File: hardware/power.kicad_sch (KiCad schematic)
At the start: 19 parts, among them U1 ECP5U_12_CABGA256, U2 TLV62569DBV, U3 TLV62569DBV, U4 TLV62569DBV

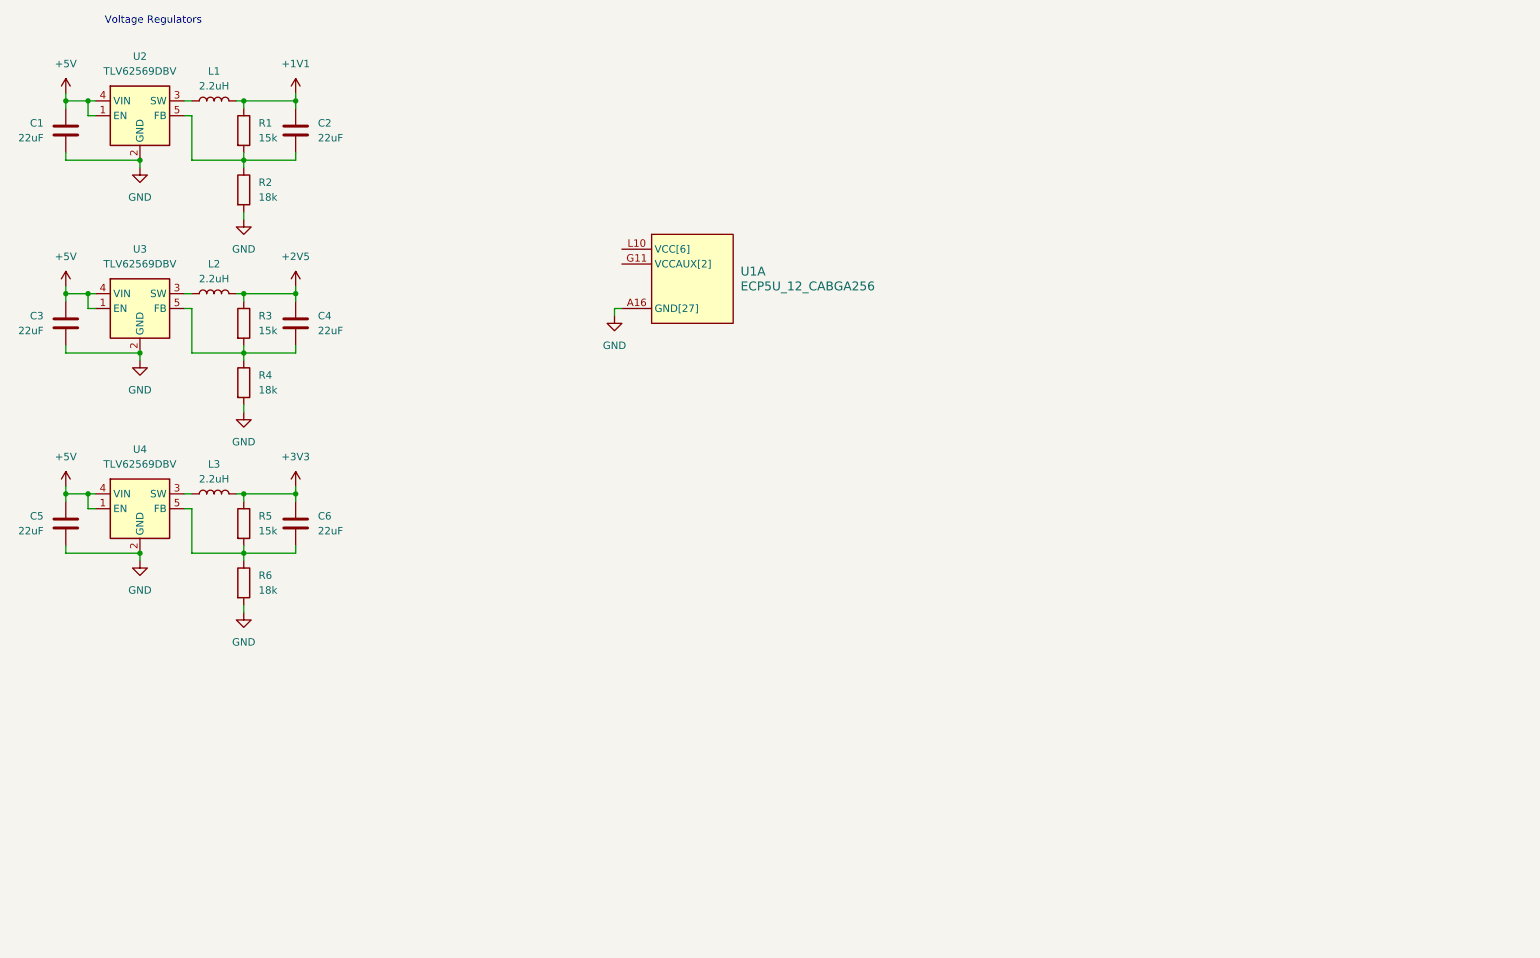
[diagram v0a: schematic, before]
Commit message: Routed most of sdram
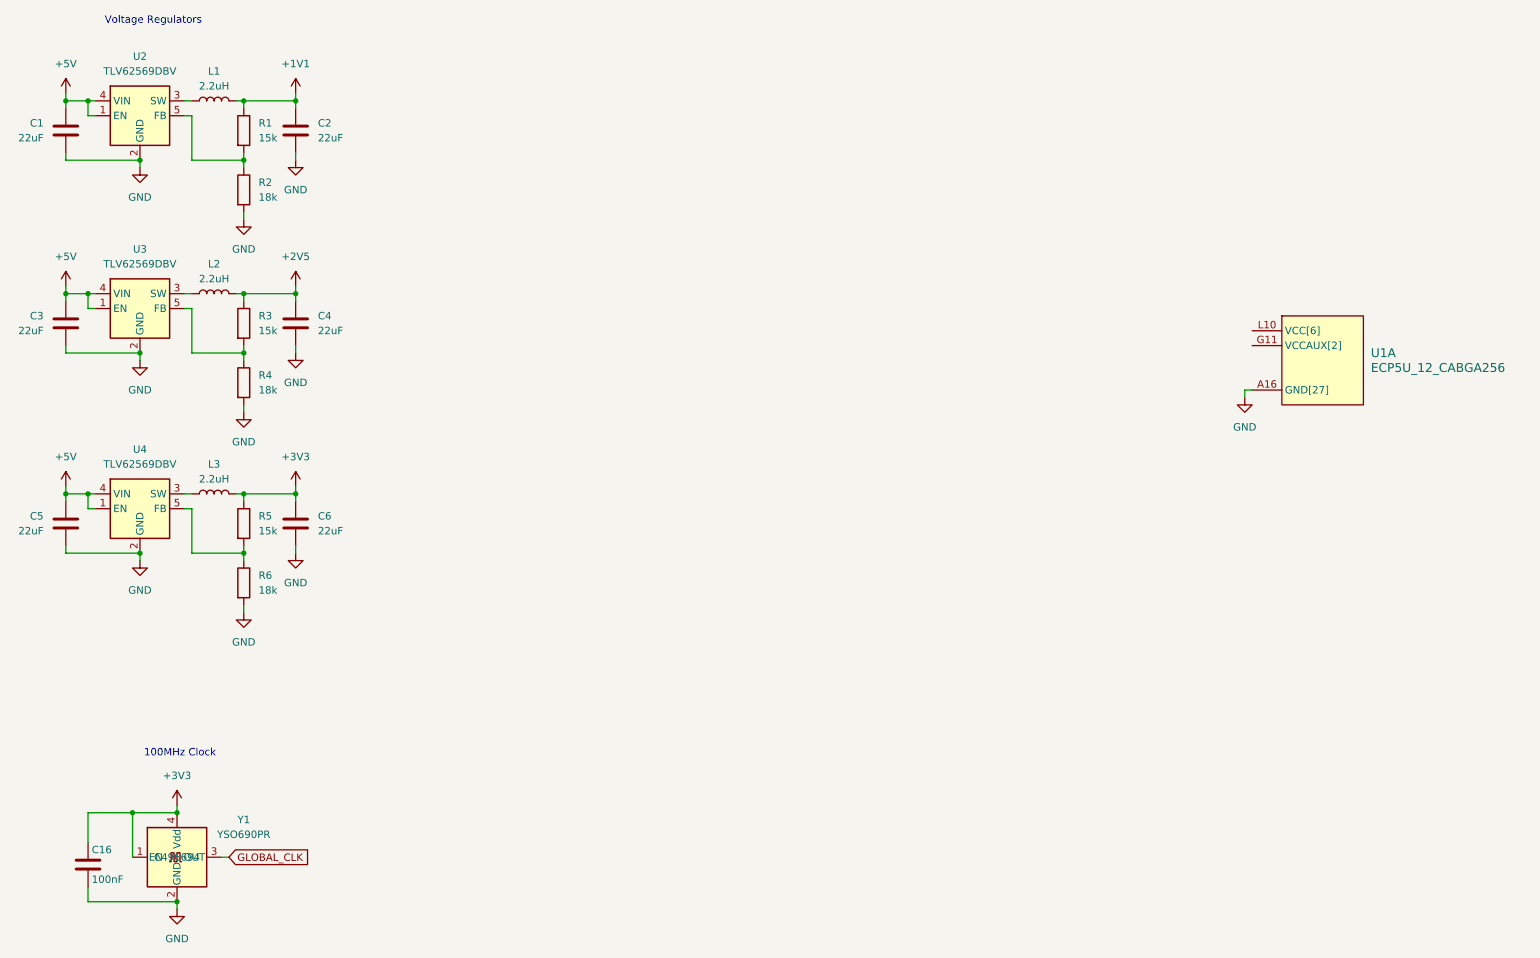
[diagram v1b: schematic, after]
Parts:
- added C16: 100nF, Capacitor_SMD:C_0402_1005Metric, symbol Device:C
- added Y1: YSO690PR, Oscillator:Oscillator_SMD_SiT_PQFN-4Pin_3.2x2.5mm, symbol Oscillator:ASE-xxxMHz
- R1, R2, R3, R4, R5, R6: footprint Resistor_SMD:R_0603_1608Metric -> Resistor_SMD:R_0402_1005Metric
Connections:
- net +3V3: now also C16.1, Y1.1 (EN), Y1.4 (Vdd)
- net GND: now also C2.2, C4.2, C6.2, C16.2, Y1.2 (GND)
- net at R1.2, R2.1, U2.5 (FB): no longer C2.2
- net at R5.2, R6.1, U4.5 (FB): no longer C6.2
- net at R3.2, R4.1, U3.5 (FB): no longer C4.2
- new net GLOBAL_CLK: Y1.3 (OUT)
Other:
- note added: "100MHz Clock"
- moved on the sheet: U1A

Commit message: Added the decoupling capacitors
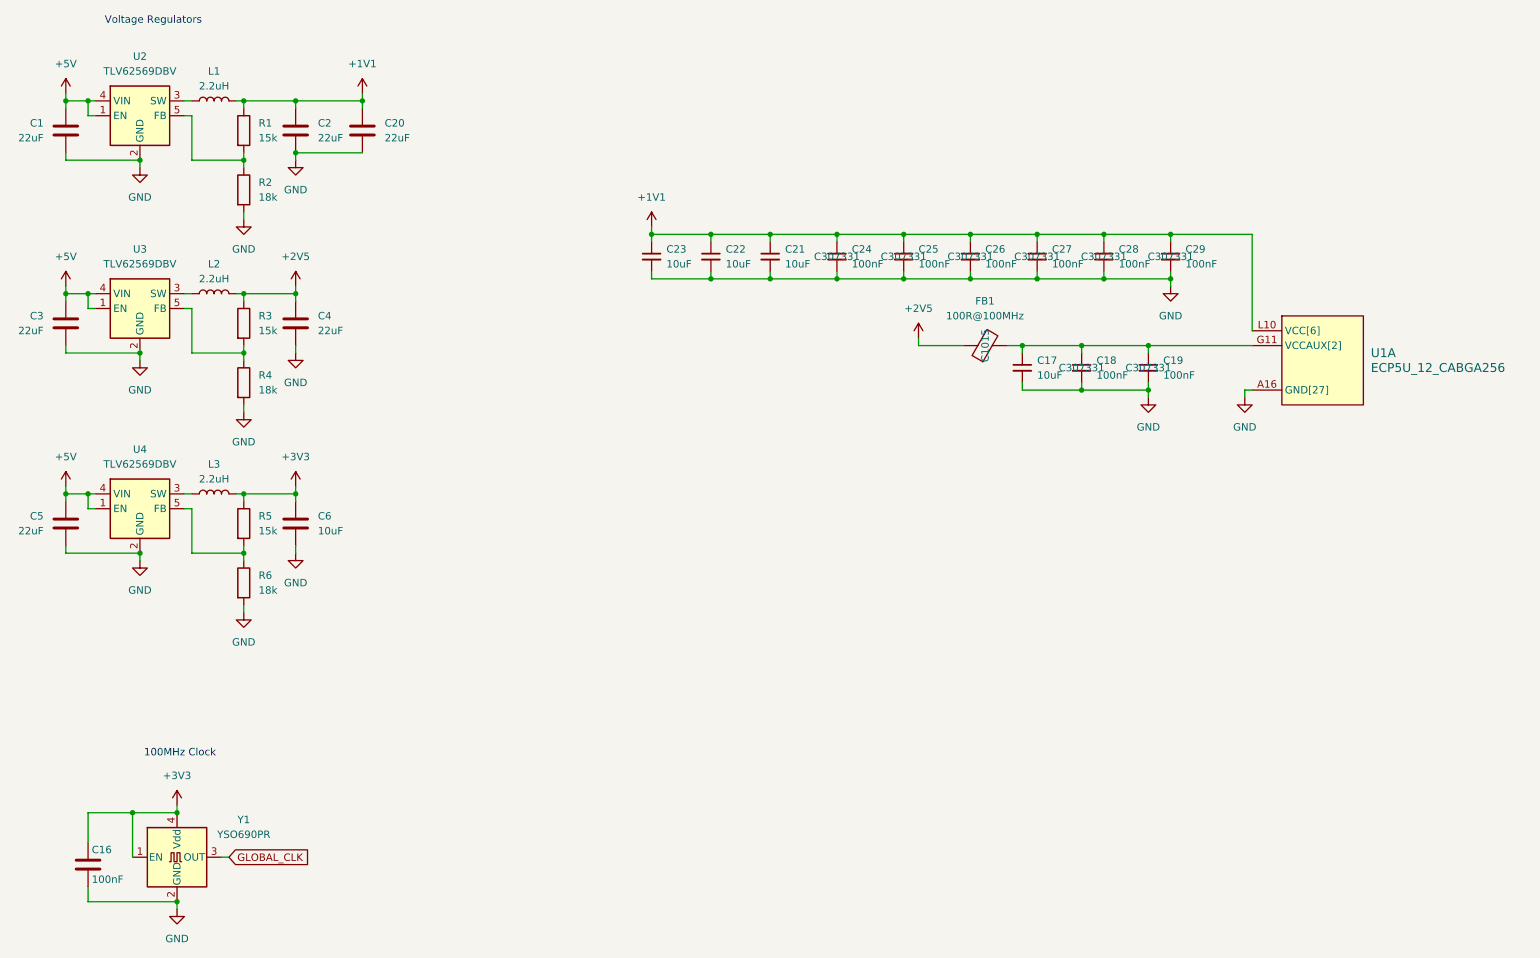
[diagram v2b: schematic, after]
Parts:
- added C17, C21, C22, C23: 10uF, Capacitor_SMD:C_0603_1608Metric, symbol Device:C_Small
- added C18, C19, C24, C25, C26, C27, C28, C29: 100nF, Capacitor_SMD:C_0402_1005Metric, symbol Device:C_Small
- added C20: 22uF, Capacitor_SMD:C_0603_1608Metric, symbol Device:C
- added FB1: 100R@100MHz, Inductor_SMD:L_0805_2012Metric, symbol Device:FerriteBead
- C1, C2, C3, C4, C5: JLCPCB Part # (none) -> C59461
- C16: JLCPCB Part # (none) -> C307331
- C6: value 22uF -> 10uF
- R1, R3, R5: JLCPCB Part # (none) -> C25756
- R2, R4, R6: JLCPCB Part # (none) -> C25762
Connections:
- net +1V1: now also U1.G6 (VCC[6]), U1.G7 (VCC[6]), U1.G9 (VCC[6]), U1.L10 (VCC[6]), U1.L8 (VCC[6]), U1.L9 (VCC[6]), C20.1, C21.1, C22.1, C23.1, C24.1, C25.1, C26.1, C27.1, C28.1, C29.1
- net +2V5: now also FB1.1
- net GND: now also C17.2, C18.2, C19.2, C20.2, C21.2, C22.2, C23.2, C24.2, C25.2, C26.2, C27.2, C28.2, C29.2
- net at U1.G11 (VCCAUX[2]), U1.L7 (VCCAUX[2]): now also C17.1, C18.1, C19.1, FB1.2

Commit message: V1.0 Final Revision and Readme documentation
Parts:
- removed Y1: YSO690PR, Oscillator:Oscillator_SMD_SiT_PQFN-4Pin_3.2x2.5mm, symbol Oscillator:ASE-xxxMHz
- added Y1: SIT8008xx-1x-xxE-100.000000, Oscillator:Oscillator_SMD_SiT_PQFN-4Pin_2.5x2.0mm, symbol Oscillator:SiT8008xx-1x-xxE
- renumbered C27 to C10, C28 to C11, C29 to C12, C3 to C13, C4 to C14, C17 to C15, C18 to C16, C19 to C17, C5 to C18, C6 to C19, C16 to C20, C20 to C3, C23 to C4, C22 to C5, C21 to C6, C24 to C7, C25 to C8, C26 to C9, R6 to R10, R1 to R5, R2 to R6, R3 to R7, R4 to R8, R5 to R9, U2 to U1, U3 to U2, U1 to U3
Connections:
- net +3V3: now also Y1.1 (OE), Y1.4 (Vdd)
- net GLOBAL_CLK: now also Y1.3 (OUT)
- net GND: now also Y1.2 (GND)
- net FILTERED_2V5: now reaches C15.1, C16.1, C17.1, FB1.2, U3.G11 (VCCAUX[2]), U3.L7 (VCCAUX[2])

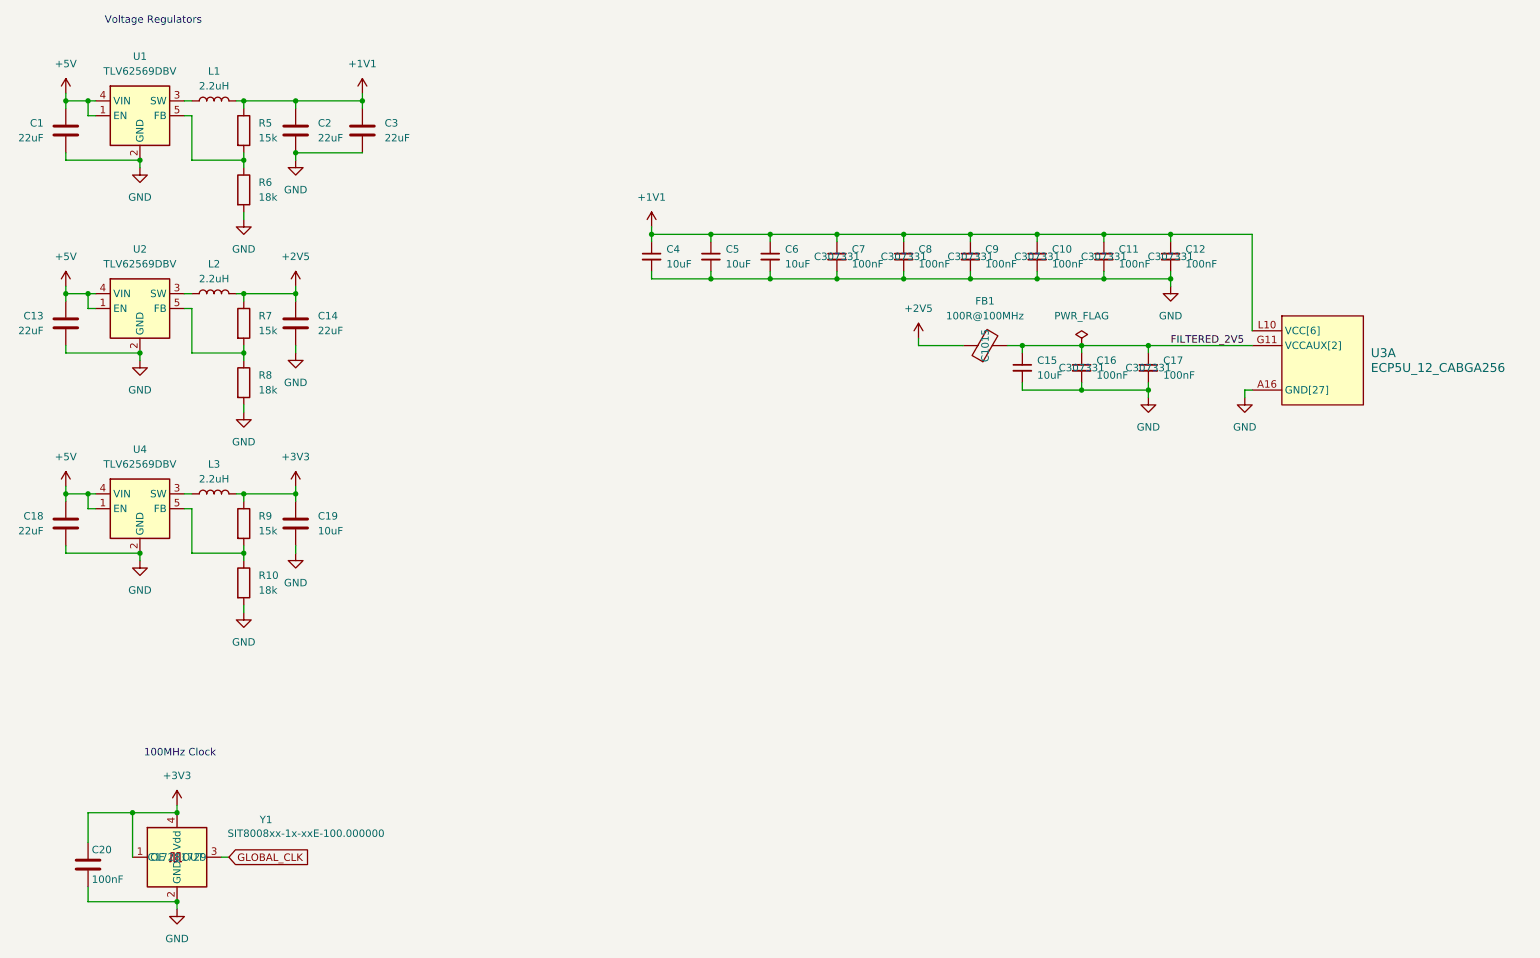
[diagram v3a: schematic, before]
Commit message: Fix level shifter EN voltage error
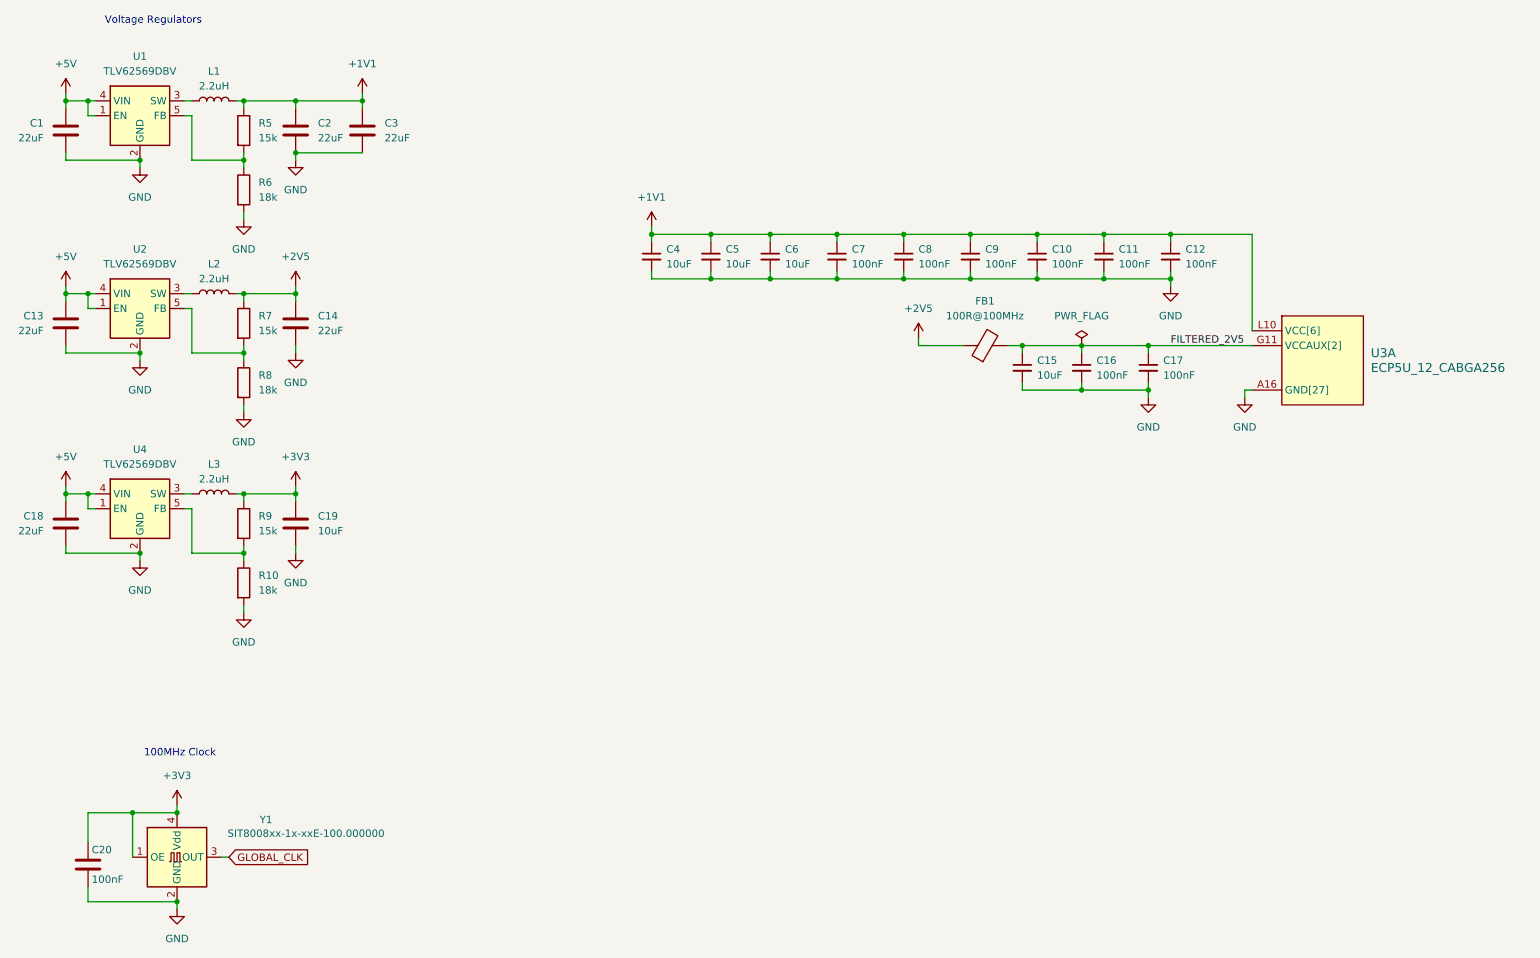
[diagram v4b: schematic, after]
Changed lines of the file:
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@@
 					(size 1.27 1.27)
 				)
+				(hide yes)
 			)
 		)
@@
 					(size 1.27 1.27)
 				)
+				(hide yes)
 			)
 		)
@@
 					(size 1.27 1.27)
 				)
+				(hide yes)
 			)
 		)
@@
 					(size 1.27 1.27)
 				)
+				(hide yes)
 			)
 		)
@@
 					(size 1.27 1.27)
 				)
+				(hide yes)
 			)
 		)
@@
 					(size 1.27 1.27)
 				)
+				(hide yes)
 			)
 		)
@@
 					(size 1.27 1.27)
 				)
+				(hide yes)
 			)
 		)
@@
 					(size 1.27 1.27)
 				)
+				(hide yes)
 			)
 		)
@@
 					(size 1.27 1.27)
 				)
+				(hide yes)
 			)
 		)
@@
 					(size 1.27 1.27)
 				)
+				(hide yes)
 			)
 		)

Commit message: Add a revision
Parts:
- added C50, C51, C52: 100nF, Capacitor_SMD:C_0402_1005Metric, symbol Device:C
- R10: value 18k -> 3.3k; JLCPCB Part # C25762 -> C25890
- R5: value 15k -> 10k; JLCPCB Part # C25756 -> C25744
- R6: value 18k -> 12k; JLCPCB Part # C25762 -> C25752
- R8: value 18k -> 4.7k; JLCPCB Part # C25762 -> C25900
- Y1: JLCPCB Part # C17281729 -> C437147
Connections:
- net +1V1: now also C50.1
- net +2V5: now also C51.1
- net +3V3: now also C52.1
- net GND: now also C50.2, C51.2, C52.2
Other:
- note added: "(10/12+1)*0.6=1.1"
- note added: "(15/3.3+1)*0.6=2.5"
- note added: "(15/4.7+1)*0.6=2.5"
- note added: "40MHz Clock"
- note removed: "100MHz Clock"

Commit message: Pre-prod fixes
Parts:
- Y1: JLCPCB Part # C437147 -> C1182928
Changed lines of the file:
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@@
 			)
 		)
-		(property "JLCPCB Part #" "C437147"
+		(property "JLCPCB Part #" "C1182928"
 			(at 43.18 158.75 0)
 			(effects
